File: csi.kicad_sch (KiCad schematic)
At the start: 101 parts, among them J7 WE_68715014522, J8 WE_68715014522, Q5 NX138BKMYL, Q6 NX138BKMYL, Q7 NX138BKMYL, Q8 NX138BKMYL, U26 PCA9547BS, U27 NX3DV642, U28 NX3DV642, U31 NTS0102GT, U32 NTS0102GT

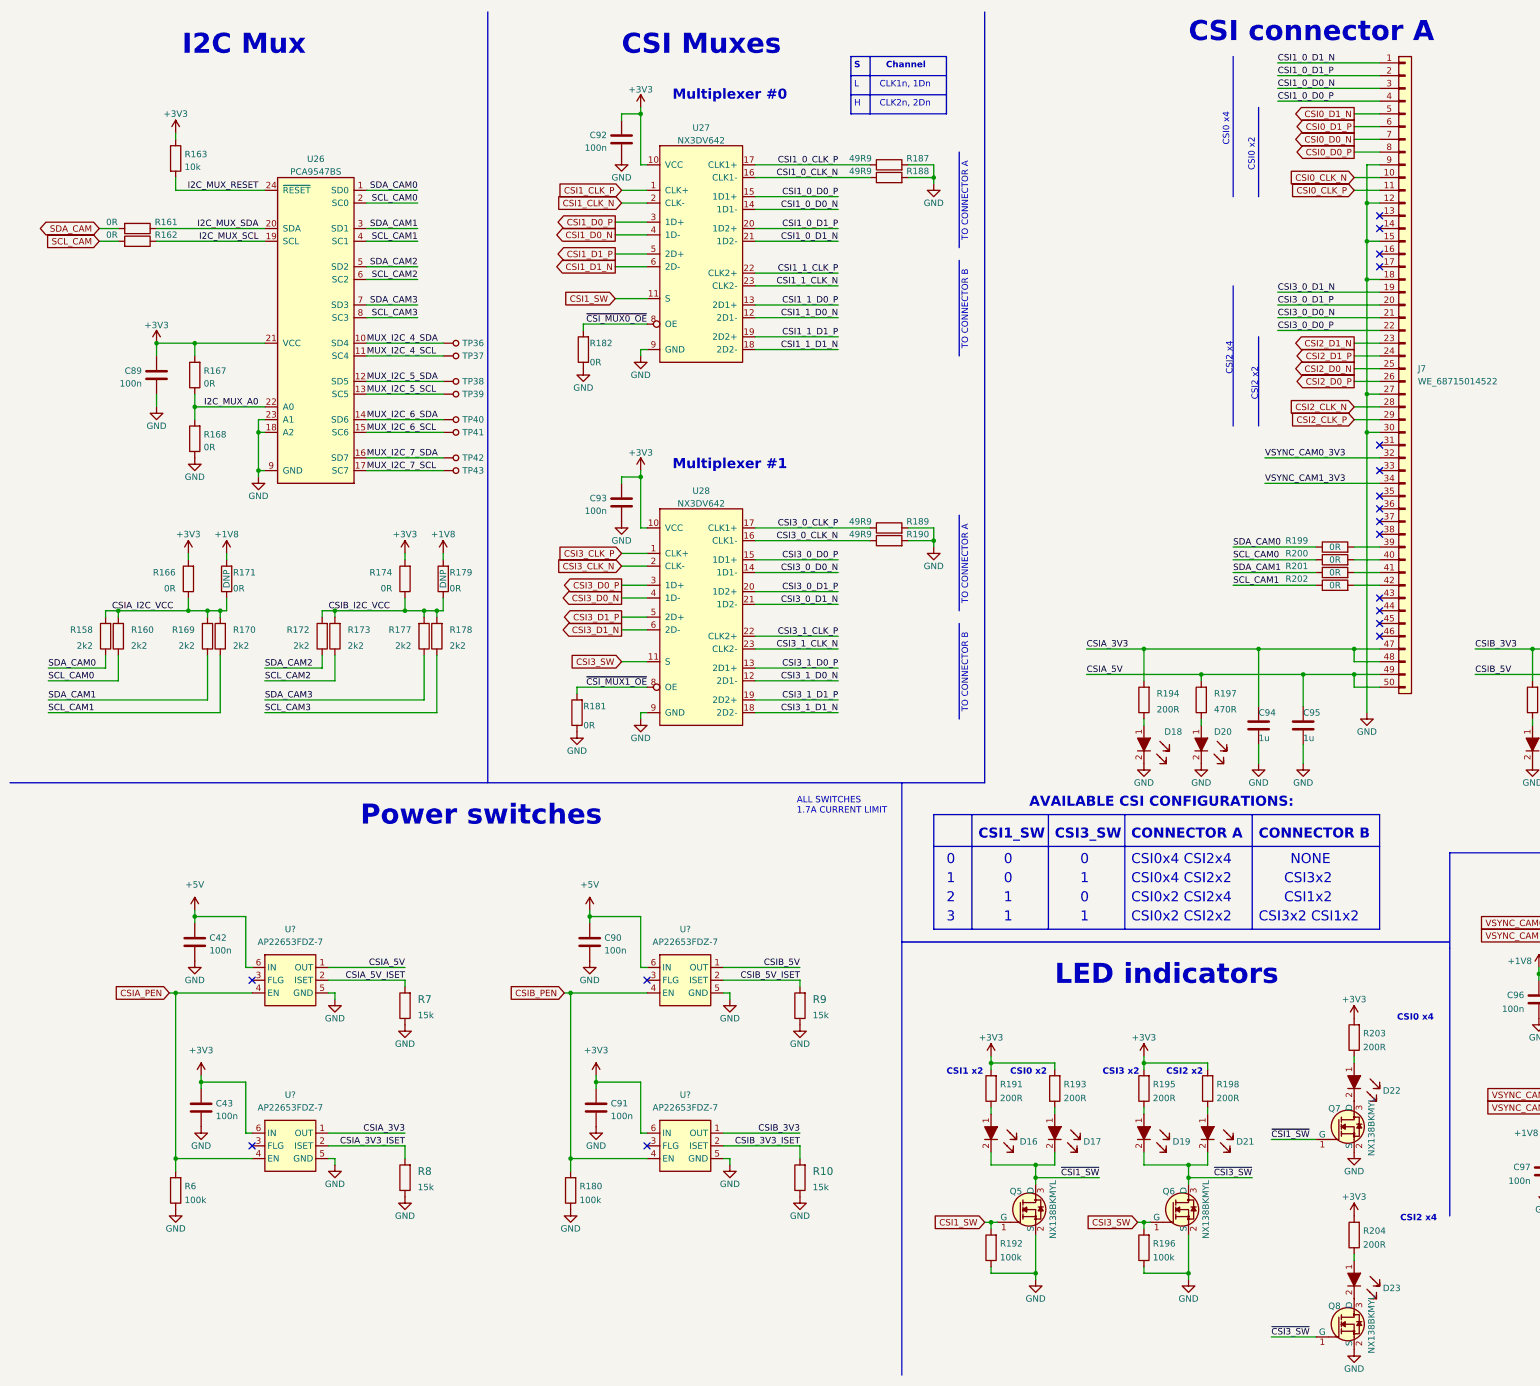
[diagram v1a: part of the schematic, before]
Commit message: Replace CSI muxes with R0s. annotate parts
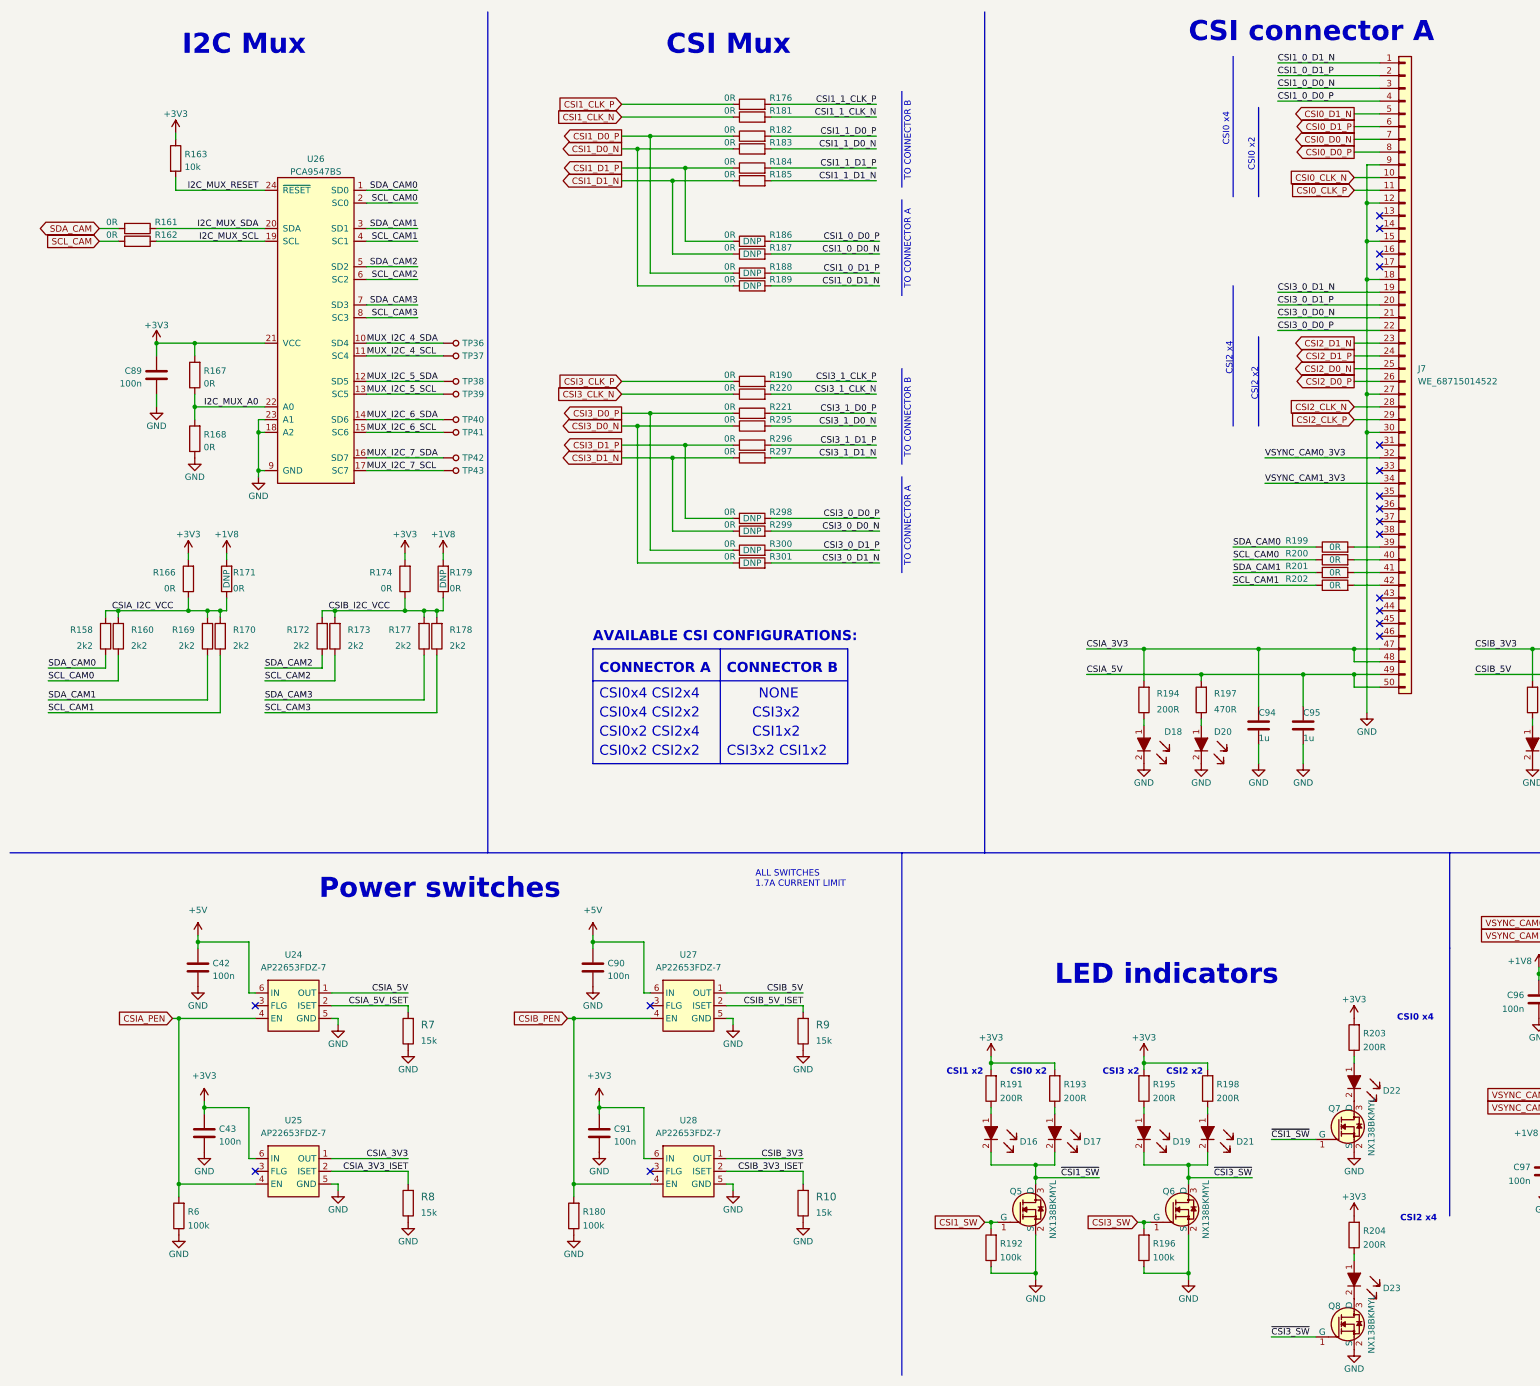
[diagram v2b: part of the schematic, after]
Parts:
- removed C92, C93: C_100n_0402, antmicro-footprints:0402-cap, symbol antmicroCapacitors0402:C_100n_0402
- removed R187, R188, R189, R190: R_49R9_0402, antmicro-footprints:0402-res, symbol antmicroResistors0402:R_49R9_0402
- removed U27, U28: NX3DV642, antmicro-footprints:QFN-24-1EP_3x4mm_P0.4mm_EP1.65x2.65mm, symbol antmicroLogicSignalSwitchesMultiplexersDecoders:NX3DV642
- added R176, R183, R184, R185, R186, R187, R188, R189, R190, R220, R221, R295, R296, R297, R298, R299, R300, R301: R_0R_0402, antmicro-footprints:0402-res, symbol antmicroResistors0402:R_0R_0402
- gave numbers to parts that had none: 4
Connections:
- net ~{CSI_MUX0_OE} is gone; now on net CSI1_1_D0_P: R182.2
- net ~{CSI_MUX1_OE} is gone; now on net CSI1_1_CLK_N: R181.2
- net CSI1_0_D0_N: now also R187.2
- net CSI1_0_D0_P: now also R186.2
- net CSI1_0_D1_N: now also R189.2
- net CSI1_0_D1_P: now also R188.2
- net CSI1_1_CLK_P: now also R176.2
- net CSI1_1_D0_N: now also R183.2
- net CSI1_1_D1_N: now also R185.2
- net CSI1_1_D1_P: now also R184.2
- net CSI1_CLK_N: now also R181.1
- net CSI1_CLK_P: now also R176.1
- net CSI1_D0_N: now also R183.1, R189.1
- net CSI1_D0_P: now also R182.1, R188.1
- net CSI1_D1_N: now also R185.1, R187.1
- net CSI1_D1_P: now also R184.1, R186.1
- net CSI3_0_D0_N: now also R299.2
- net CSI3_0_D0_P: now also R298.2
- net CSI3_0_D1_N: now also R301.2
- net CSI3_0_D1_P: now also R300.2
- net CSI3_1_CLK_N: now also R220.2
- net CSI3_1_CLK_P: now also R190.2
- net CSI3_1_D0_N: now also R295.2
- net CSI3_1_D0_P: now also R221.2
- net CSI3_1_D1_N: now also R297.2
- net CSI3_1_D1_P: now also R296.2
- net CSI3_CLK_N: now also R220.1
- net CSI3_CLK_P: now also R190.1
- net CSI3_D0_N: now also R295.1, R301.1
- net CSI3_D0_P: now also R221.1, R300.1
- net CSI3_D1_N: now also R297.1, R299.1
- net CSI3_D1_P: now also R296.1, R298.1
- net GND: no longer R181.1, R182.1
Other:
- note added: "CSI Mux"
- note removed: "0"
- note removed: "1"
- note removed: "2"
- note removed: "3"
- note removed: "CLK1n, 1Dn"
- note removed: "CLK2n, 2Dn"
- note removed: "CSI Muxes"
- note removed: "CSI1_SW"
- note removed: "CSI3_SW"
- note removed: "Channel"
- note removed: "H"
- note removed: "L"
- note removed: "Multiplexer #0"
- note removed: "Multiplexer #1"
- note removed: "S"
- moved on the sheet: C42, C43, C90, C91, R10, R180, R6, R7, R8, R9, U24, U25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

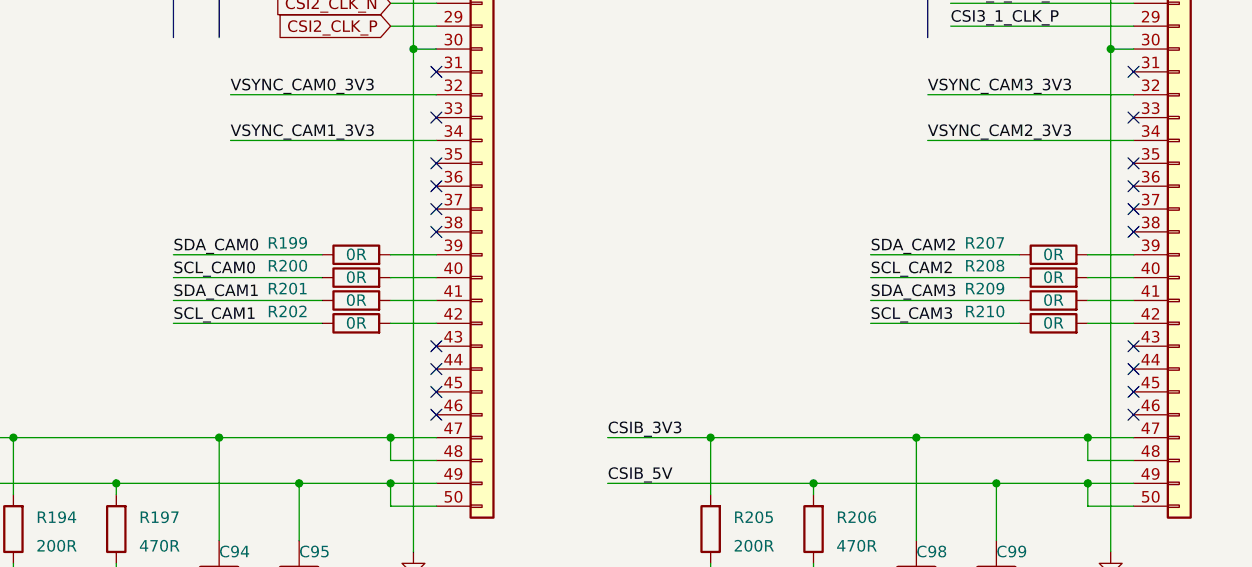
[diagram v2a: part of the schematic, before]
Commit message: Remove R0s from high speed signals, replace part of R0s with resistor ladder. Assign net clases
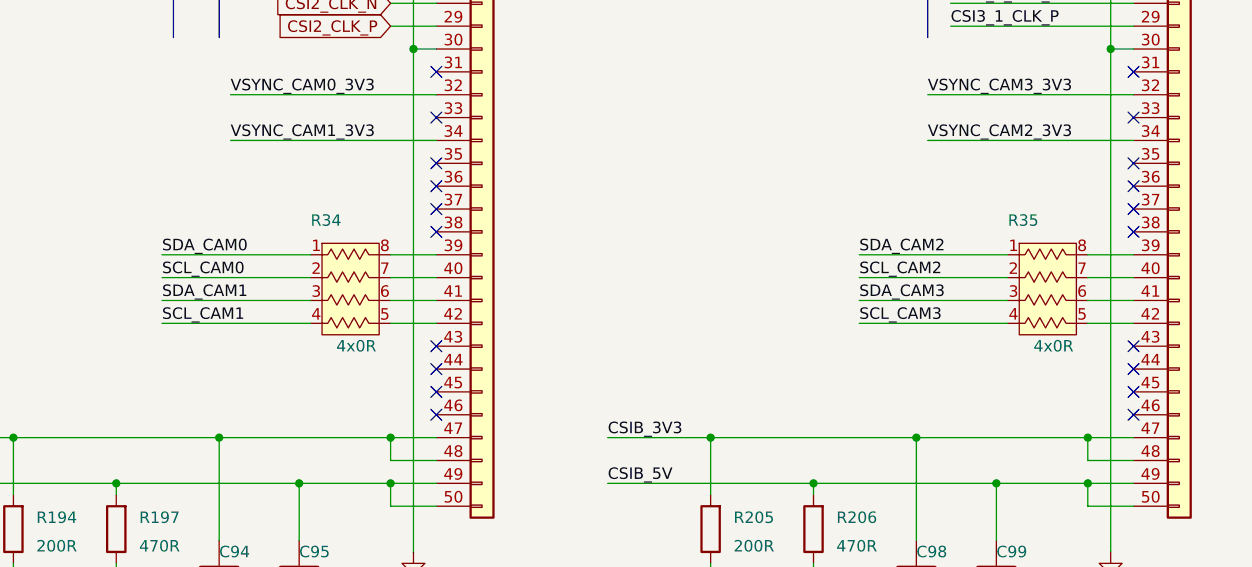
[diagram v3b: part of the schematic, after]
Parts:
- removed R199, R200, R201, R202, R207, R208, R209, R210: R_0R_0402, antmicro-footprints:0402-res, symbol antmicroResistors0402:R_0R_0402
- added R34, R35: 4x0R_0201_array, antmicro-footprints:EXB18V, symbol antmicroResistorNetworksArrays:4x0R_0201_array
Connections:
- net SCL_CAM0: now also R34.2
- net SCL_CAM1: now also R34.4
- net SCL_CAM2: now also R35.2
- net SCL_CAM3: now also R35.4
- net SDA_CAM0: now also R34.1
- net SDA_CAM1: now also R34.3
- net SDA_CAM2: now also R35.1
- net SDA_CAM3: now also R35.3
- net at J7.42 (Pin_42): now also R34.5
- net at J7.40 (Pin_40): now also R34.7
- net at J8.39 (Pin_39): now also R35.8
- net at J8.40 (Pin_40): now also R35.7
- net at J8.41 (Pin_41): now also R35.6
- net at J8.42 (Pin_42): now also R35.5
- net at J7.39 (Pin_39): now also R34.8
- net at J7.41 (Pin_41): now also R34.6

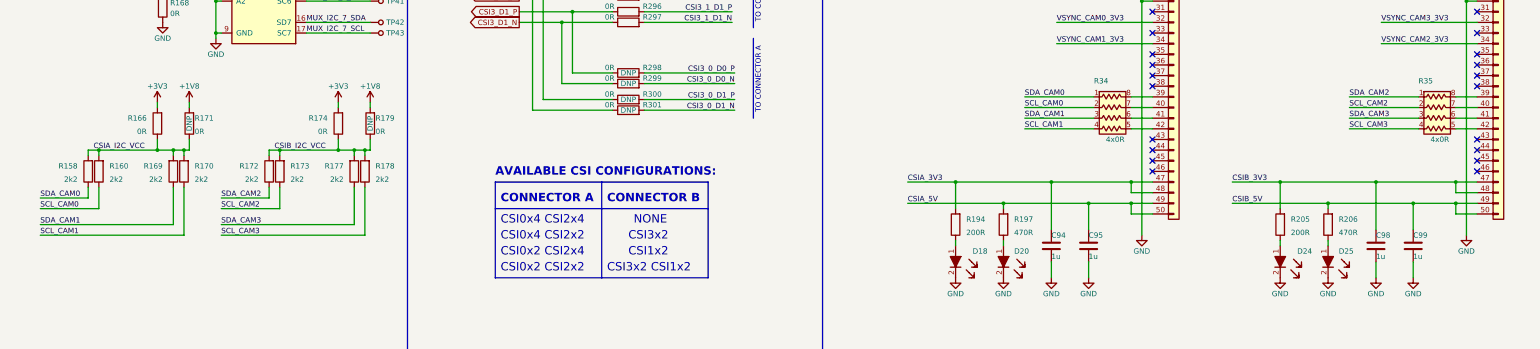
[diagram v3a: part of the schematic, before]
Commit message: Replace I2C pullups with 2.2kOhm array
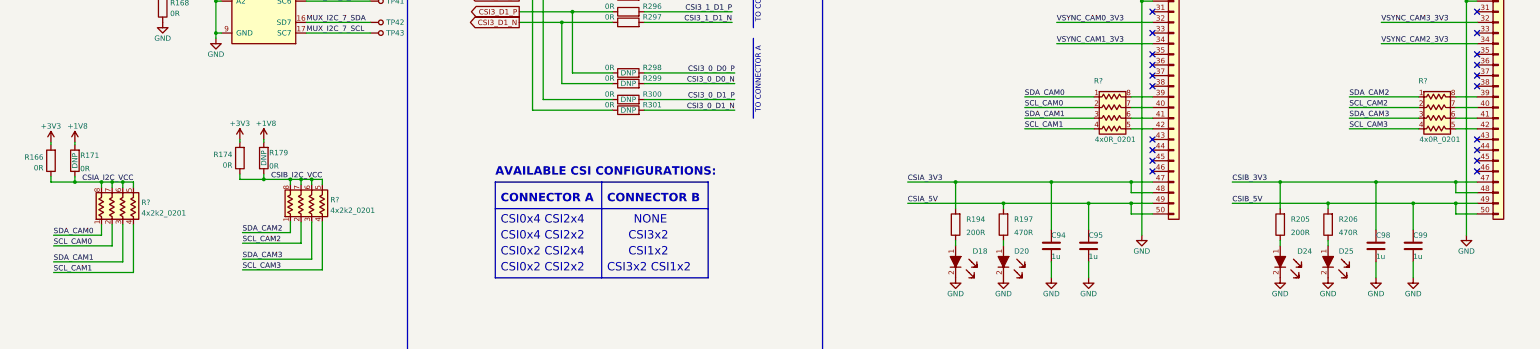
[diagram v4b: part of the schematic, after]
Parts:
- removed R158, R160, R169, R170, R172, R173, R177, R178: R_2k2_0402, antmicro-footprints:0402-res, symbol antmicroResistors0402:R_2k2_0402
- added R? (x2): 4x2k2_0201_array, antmicro-footprints:EXB18V, symbol antmicroResistorNetworksArrays:4x2k2_0201_array
- R?: renamed from R34; Val 4x0R -> 4x0R_0201
- R?: renamed from R35; Val 4x0R -> 4x0R_0201
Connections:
- net CSIA_I2C_VCC: now also R?.5, R?.6, R?.7, R?.8
- net CSIB_I2C_VCC: now also R?.5, R?.6, R?.7, R?.8
- net SCL_CAM0: now also R?.2
- net SCL_CAM1: now also R?.4
- net SCL_CAM2: now also R?.2
- net SCL_CAM3: now also R?.4
- net SDA_CAM0: now also R?.1
- net SDA_CAM1: now also R?.3
- net SDA_CAM2: now also R?.1
- net SDA_CAM3: now also R?.3
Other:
- moved on the sheet: R166, R171, R174, R179
